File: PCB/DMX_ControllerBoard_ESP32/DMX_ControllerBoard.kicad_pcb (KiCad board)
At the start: 4 copper layers, 100 x 36.8 mm, 41 parts, among them J1 Screw_Terminal_01x03, J2 Screw_Terminal_01x03, J3 PWR_IN, J4 Screw_Terminal_01x03, J5 Conn_Left, J6 Screw_Terminal_01x03, J7 ProgrammingHeader, SW1 SW_SPST, SW2 SW_SPST, SW3 SW_SPST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

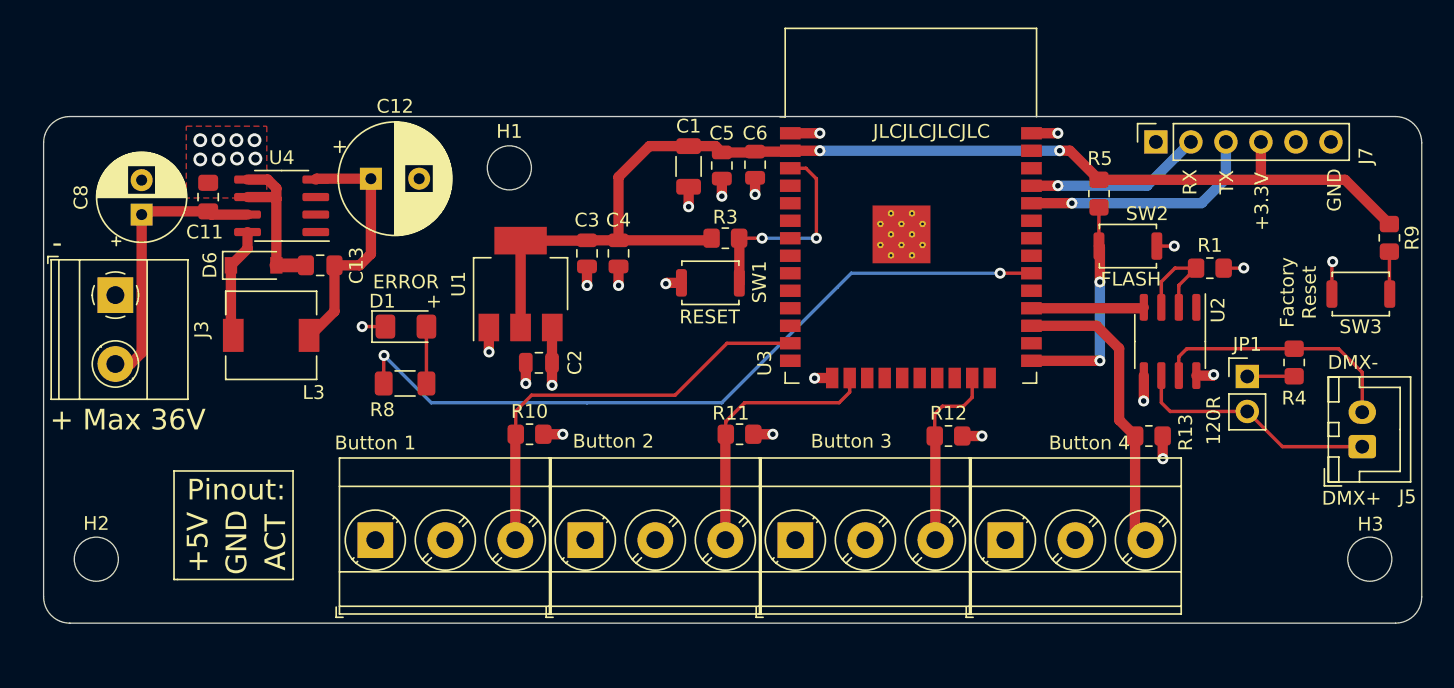
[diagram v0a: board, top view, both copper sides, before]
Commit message: Added more labeling to ESP32 board
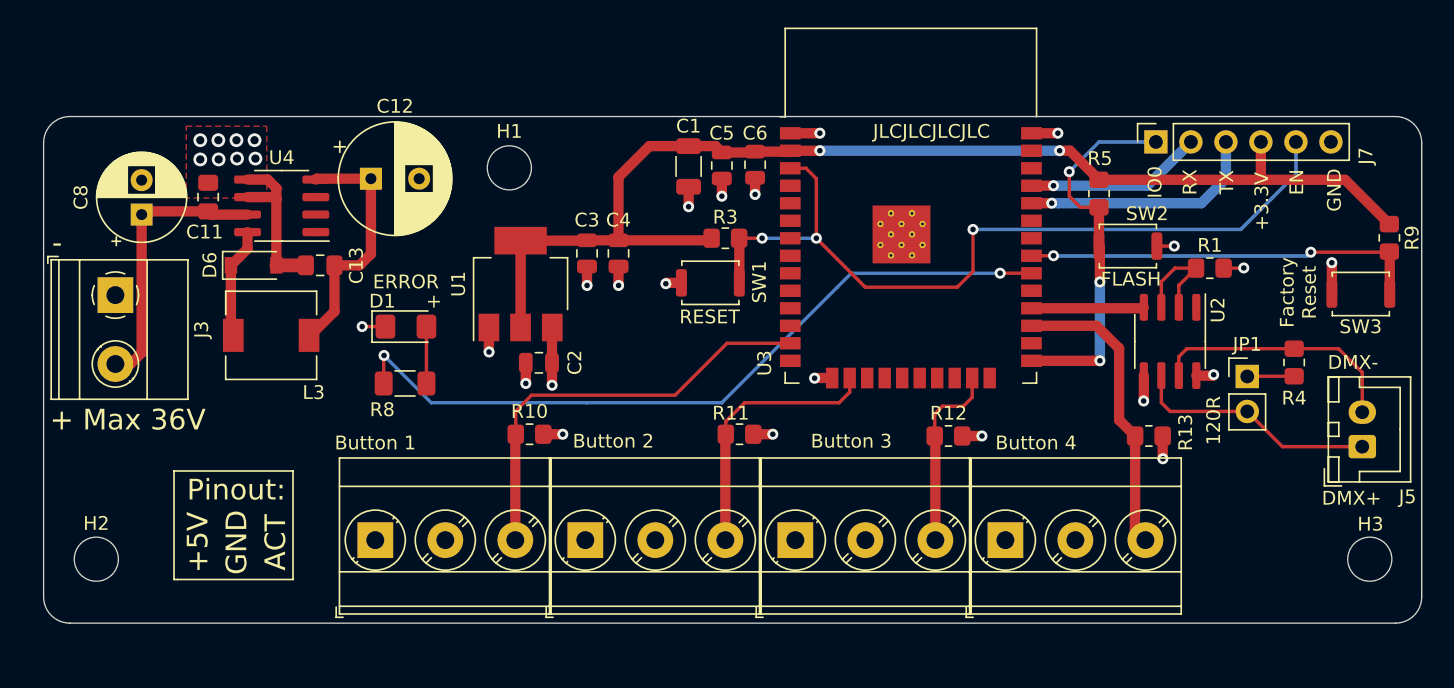
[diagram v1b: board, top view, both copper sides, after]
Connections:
- J7 pad 1: unconnected-(J7-Pad1) -> BOOT_MODE
- J7 pad 5: unconnected-(J7-Pad5) -> RESET
- U3 pad 31: unconnected-(U3-Pad31) -> FACTORY_RESET
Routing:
- net RESET: track 15.4 -> 59.2 mm, vias 2 -> 3
- net FACTORY_RESET: track 3.18 -> 29.2 mm, vias 0 -> 2
- net BOOT_MODE: track 16.1 -> 27.6 mm, vias 2 -> 3
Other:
- board text added: "DMX Controller Board V2.0"
- board text added: "EN"
- board text added: "IO0"
- board text removed: "DMX Controller Board V1.1"

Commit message: Initial commit of ESP32 based PCB
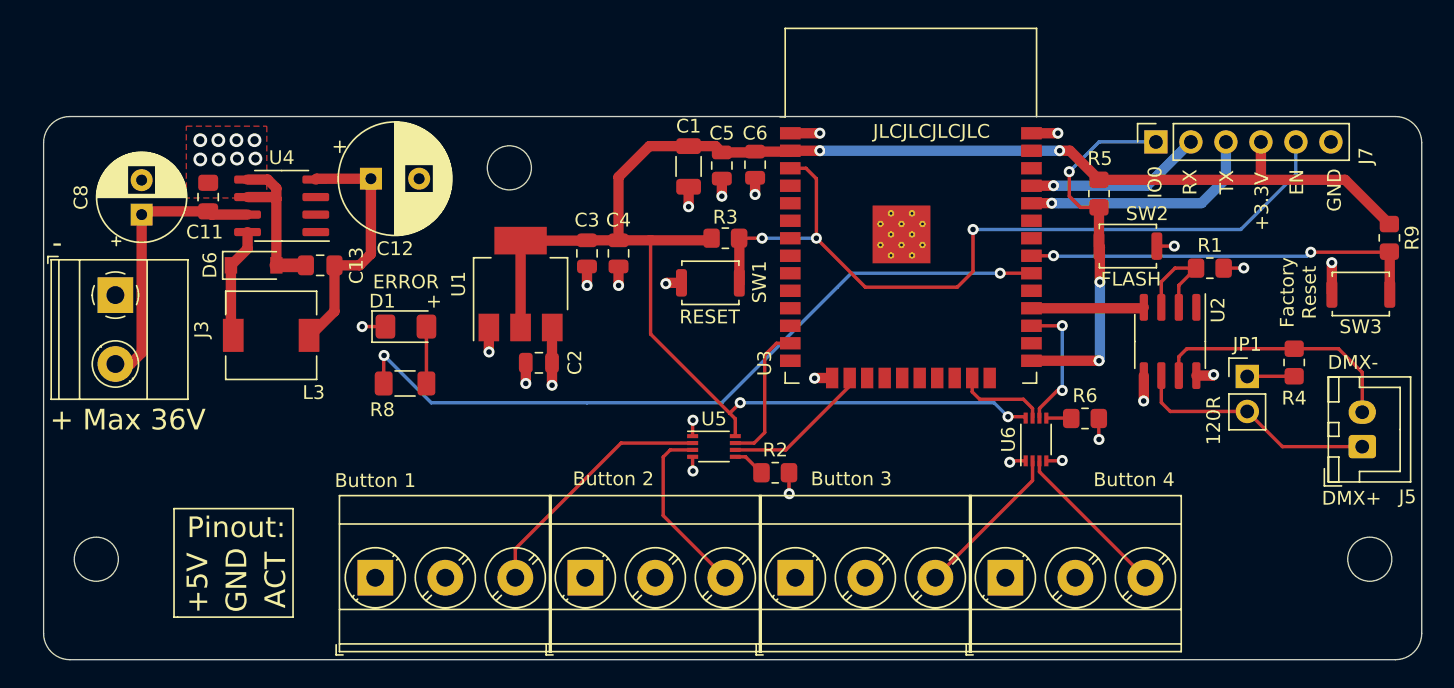
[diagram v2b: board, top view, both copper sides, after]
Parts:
- removed R10, R11, R12, R13: 10k, Resistor_SMD:R_0805_2012Metric_Pad1.20x1.40mm_HandSolder
- added R2: 10k, Resistor_SMD:R_0805_2012Metric_Pad1.20x1.40mm_HandSolder, F.Cu at (72.1, 51.4)
- added R6: 10k, Resistor_SMD:R_0805_2012Metric_Pad1.20x1.40mm_HandSolder, F.Cu at (94.6, 47.5)
- added U5: 74LVC2T45DC, Package_SO:VSSOP-8_2.3x2mm_P0.5mm, F.Cu at (67.7, 49.5)
- added U6: 74LVC2T45DC, Package_SO:VSSOP-8_2.3x2mm_P0.5mm, F.Cu at (91.1, 49.0)
- moved J1 2.73 mm to (43.1, 59.1)
- moved J2 2.73 mm to (58.4, 59.1)
- moved J4 2.73 mm to (73.6, 59.1)
- moved J6 2.73 mm to (88.8, 59.1)
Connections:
- net +3V3 renamed +3.3V
- J1 pad 3: B1 -> Button1_sense
- J2 pad 3: B2 -> Button2_sense
- J4 pad 3: B3 -> Button3_sense
- J6 pad 3: B4 -> Button4_sense
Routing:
- net +3.3V: track 86.9 -> 125.9 mm, vias 2 -> 4
- net B1: track 31.3 -> 10.3 mm
- net Button1_sense: track 0.00 -> 18.1 mm
- net Button2_sense: track 0.00 -> 13.0 mm
- net B4: track 21.8 -> 9.83 mm, vias 0 -> 2
- net Button4_sense: track 0.00 -> 11.7 mm
- net Button3_sense: track 0.00 -> 11.4 mm
- net B2: track 19.6 -> 10.8 mm
- net B3: track 13.8 -> 6.58 mm
- net +5V: track 25.3 -> 30.8 mm, vias 3 -> 7
- net GND: track 41.7 -> 38.0 mm, vias 27 -> 25
- net Net-(R2-Pad1): track 0.00 -> 2.37 mm
- net Net-(R6-Pad1): track 0.00 -> 1.82 mm
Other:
- board size 100 x 36.8 mm -> 100 x 39.4 mm

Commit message: Updated labels on PCB for better readability
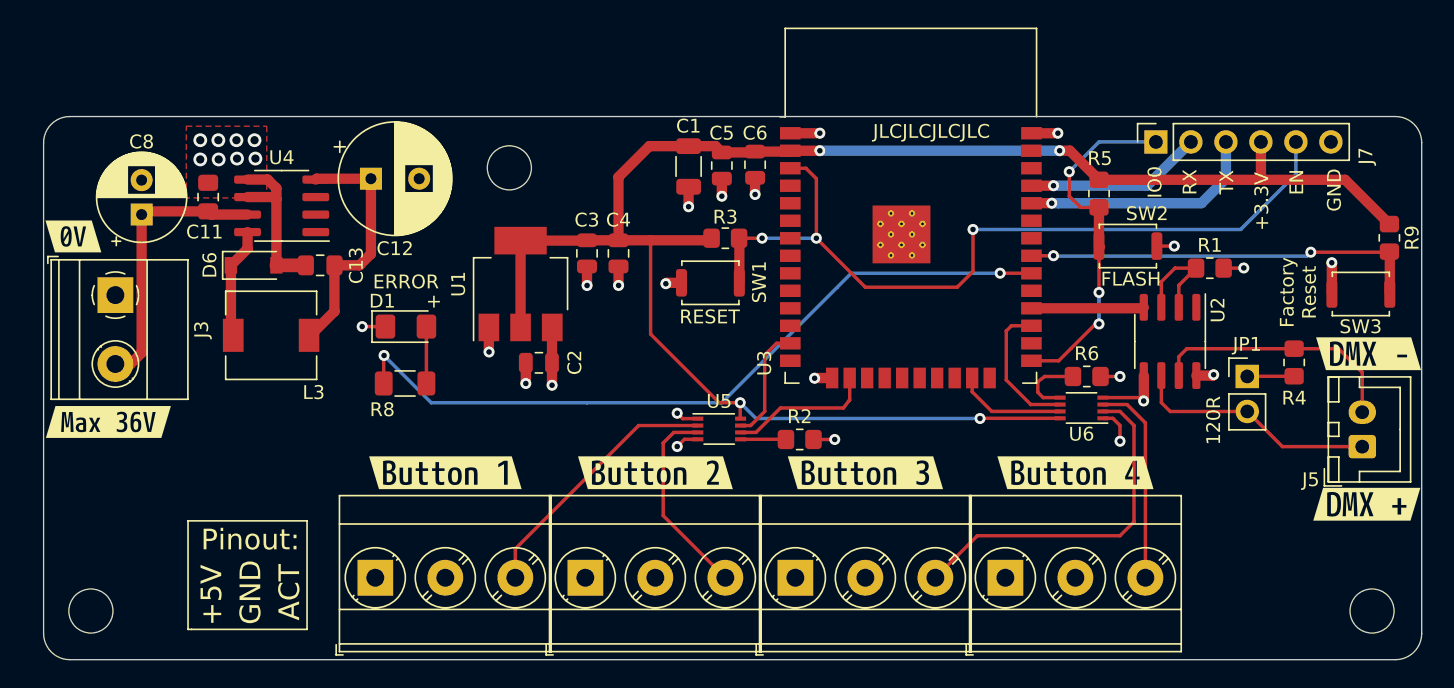
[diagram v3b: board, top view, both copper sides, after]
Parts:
- added kibuzzard-63869759: G***, kibuzzard-63869759, F.Cu at (48.2, 51.4)
- added kibuzzard-63869791: G***, kibuzzard-63869791, F.Cu at (63.4, 51.4)
- added kibuzzard-6386984B: G***, kibuzzard-6386984B, F.Cu at (78.7, 51.4)
- added kibuzzard-638699ED: G***, kibuzzard-638699ED, F.Cu at (93.9, 51.4)
- added kibuzzard-63869B9D: G***, kibuzzard-63869B9D, F.Cu at (115.1, 53.7)
- added kibuzzard-63869BC5: G***, kibuzzard-63869BC5, F.Cu at (115.2, 42.8)
- added kibuzzard-63869BE0: G***, kibuzzard-63869BE0, F.Cu at (21.2, 34.3)
- added kibuzzard-63869BE9: G***, kibuzzard-63869BE9, F.Cu at (23.7, 47.8)
- moved U6 4.02 mm to (94.4, 46.7), turned to 180 degrees
- moved H2 3.78 mm to (22.5, 61.5)
- moved H3 3.76 mm to (115.4, 61.5)
- moved R6 3.05 mm to (94.7, 44.5)
- moved R2 3.00 mm to (73.9, 49.0)
- moved U5 1.33 mm to (68.1, 48.3)
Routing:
- net Button3_sense: track 11.4 -> 25.8 mm
- net Net-(R6-Pad1): track 1.82 -> 5.23 mm
- net Button4_sense: track 11.7 -> 14.9 mm
- net GND: track 38.0 -> 40.6 mm, vias 25 -> 24
- net B1: track 10.3 -> 8.48 mm
- net +5V: track 30.8 -> 32.5 mm
- net BOOT_MODE: track 27.5 -> 26.0 mm
- net Button2_sense: track 13.0 -> 14.5 mm
- net B3: track 6.58 -> 7.97 mm
- net +3.3V: track 125.9 -> 127.2 mm
- net Net-(R2-Pad1): track 2.37 -> 3.30 mm
- net Button1_sense: track 18.1 -> 19.0 mm
- net B4: track 9.83 -> 10.2 mm, vias 2 -> 0
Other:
- board text removed: "+ Max 36V"
- board text removed: "-"
- board text removed: "Button 1"
- board text removed: "Button 2"
- board text removed: "Button 3"
- board text removed: "Button 4"
- board text removed: "DMX+"
- board text removed: "DMX-"
